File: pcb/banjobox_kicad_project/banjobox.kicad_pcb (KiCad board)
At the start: 2 copper layers, 0 parts

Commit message: added voltage regulator to schematic and finished assigning footprints
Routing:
- removed copper zone on F.Cu, net (none)
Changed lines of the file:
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@@
 		)
 	)
-	(gr_rect
-		(start 131.064 84.328)
-		(end 201.676 121.92)
+	(gr_line
+		(start 51.308 47.244)
+		(end 164.084 33.528)
 		(stroke
-			(width 0.2)
+			(width 0.1)
 			(type default)
 		)
-		(fill no)
-		(layer "F.Cu")
+		(layer "User.1")
 	)
-	(zone
-		(layer "F.Cu")
-		(hatch edge 0.5)
-		(connect_pads
-			(clearance 0.5)
+	(gr_line
+		(start 164.084 33.528)
+		(end 164.084 160.02)
+		(stroke
+			(width 0.1)
+			(type default)
 		)
-		(min_thickness 0.25)
-		(fill
-			(thermal_gap 0.5)
-			(thermal_bridge_width 0.5)
-			(island_removal_mode 1)
+		(layer "User.1")
+	)
+	(gr_line
+		(start 164.084 160.02)
+		(end 51.308 47.244)
+		(stroke
+			(width 0.1)
+			(type default)
 		)
-		(polygon
-			(pts
-				(xy 201.676 84.328) (xy 131.064 84.328) (xy 131.064 121.92) (xy 201.676 121.92)
+		(layer "User.1")
+	)
+	(dimension
+		(type orthogonal)
+		(layer "Edge.Cuts")
+		(pts
+			(xy 164.084 33.528) (xy 164.084 160.02)
+		)
+		(height 11.684)
+		(orientation 1)
+		(format
+			(prefix "")
+			(suffix "")
+			(units 3)
+			(units_format 0)
+			(precision 4)
+			(suppress_zeroes yes)
+		)
+		(style
+			(thickness 0.05)
+			(arrow_length 1.27)
+			(text_position_mode 0)
+			(arrow_direction outward)
+			(extension_height 0.58642)
+			(extension_offset 0.5)
+			(keep_text_aligned yes)
+		)
+		(gr_text "126.492"
+			(at 174.618 96.774 90)
+			(layer "Edge.Cuts")
+			(effects
+				(font
+					(size 1 1)
+					(thickness 0.15)
+				)
 			)
 		)
+	)
+	(dimension
+		(type orthogonal)
+		(layer "User.1")
+		(pts
+			(xy 164.084 160.02) (xy 51.308 47.244)
+		)
+		(height 6.096)
+		(orientation 0)
+		(format
+			(prefix "")
+			(suffix "")
+			(units 3)
+			(units_format 0)
+			(precision 4)
+			(suppress_zeroes yes)
+		)
+		(style
+			(thickness 0.1)
+			(arrow_length 1.27)
+			(text_position_mode 0)
+			(arrow_direction outward)
+			(extension_height 0.58642)
+			(extension_offset 0.5)
+			(keep_text_aligned yes)
+		)
+		(gr_text "112.776"
+			(at 107.696 164.966 0)
+			(layer "User.1")
+			(effects
+				(font
+					(size 1 1)
+					(thickness 0.15)
+				)
+			)
+		)

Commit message: removed R pin from SHT31 to better suit breakout board
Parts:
- added C1: 1uF, Capacitor_THT:CP_Radial_D6.3mm_P2.50mm, F.Cu at (158.8, 117.1)
- added C2: 10uF, Capacitor_THT:CP_Radial_D6.3mm_P2.50mm, F.Cu at (138.5, 130.8)
- added C3: 100nF, Capacitor_THT:C_Disc_D3.4mm_W2.1mm_P2.50mm, F.Cu at (146.8, 136.4)
- added C4: 100nF, Capacitor_THT:C_Disc_D3.4mm_W2.1mm_P2.50mm, F.Cu at (93.5, 83.3)
- added C5: 100nF, Capacitor_THT:C_Disc_D3.4mm_W2.1mm_P2.50mm, F.Cu at (80.3, 59.1)
- added C6: 10uF, Capacitor_THT:CP_Radial_D6.3mm_P2.50mm, F.Cu at (144.8, 72.9)
- added C7: 100uF, Capacitor_THT:CP_Radial_D6.3mm_P2.50mm, F.Cu at (152.9, 73.2)
- added C8: 10uF, Capacitor_THT:CP_Radial_D6.3mm_P2.50mm, F.Cu at (123.5, 91.7)
- added C9: 10uF, Capacitor_THT:CP_Radial_D6.3mm_P2.50mm, F.Cu at (114.8, 95.0)
- added R1: 4.7k, Resistor_THT:R_Axial_DIN0207_L6.3mm_D2.5mm_P7.62mm_Horizontal, F.Cu at (102.9, 71.1)
- added R2: 4.7k, Resistor_THT:R_Axial_DIN0207_L6.3mm_D2.5mm_P7.62mm_Horizontal, F.Cu at (119.4, 71.4)
- added R3: 100k, Resistor_THT:R_Axial_DIN0207_L6.3mm_D2.5mm_P7.62mm_Horizontal, F.Cu at (138.2, 120.1)
- added REF**: TestPoint_THTPad_D3.0mm_Drill1.5mm, TestPoint:TestPoint_THTPad_D3.0mm_Drill1.5mm, F.Cu at (105.2, 94.7)
- added REF**: TestPoint_THTPad_D3.0mm_Drill1.5mm, TestPoint:TestPoint_THTPad_D3.0mm_Drill1.5mm, F.Cu at (101.1, 90.7)
- added RV1: 10K, Potentiometer_THT:Potentiometer_Runtron_RM-065_Vertical, F.Cu at (154.5, 140.5)
- added SW1: RotaryEncoder_Switch, Rotary_Encoder:RotaryEncoder_Alps_EC11E-Switch_Vertical_H20mm, F.Cu at (131.9, 53.1)
- added U2: MOUDLE-SEEEDUINO-XIAO, footprints:XIAO-Generic-Hybrid-14P-2.54-21X17.8MM, B.Cu at (149.9, 90.9)
- added U3: ER_OLEDM0.91_1x-I2C, Display:ER_OLEDM0.91_1x-I2C, F.Cu at (89.4, 59.2)
- added U5: LM1117T-3.3, Package_TO_SOT_THT:TO-220-3_Vertical, F.Cu at (112.5, 83.3)
- added U6: PAM8302AAD, Package_SO:SOIC-8_3.9x4.9mm_P1.27mm, F.Cu at (152.3, 127.9)
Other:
- board text added: "0V"
- board text added: "4.5V"

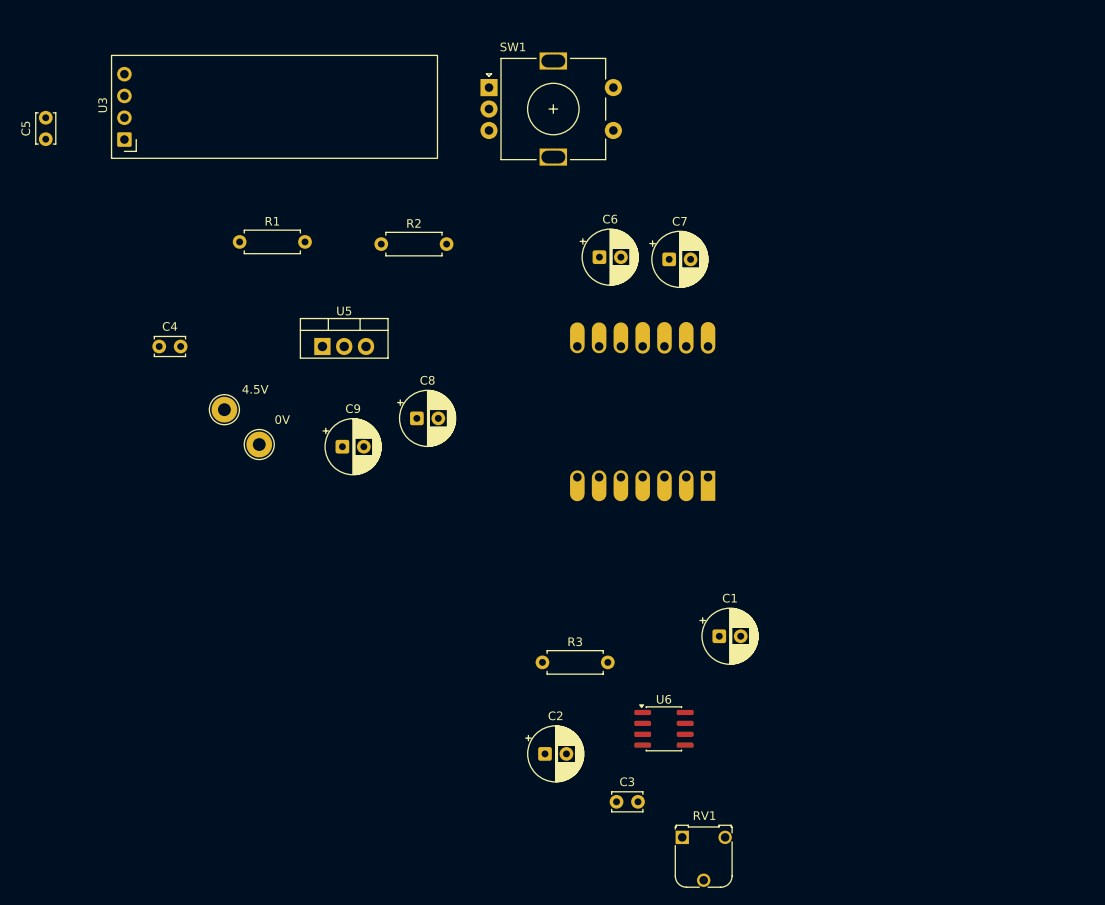
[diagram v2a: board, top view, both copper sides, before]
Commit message: assigned new footprints (pinheader) and more progress on pcb
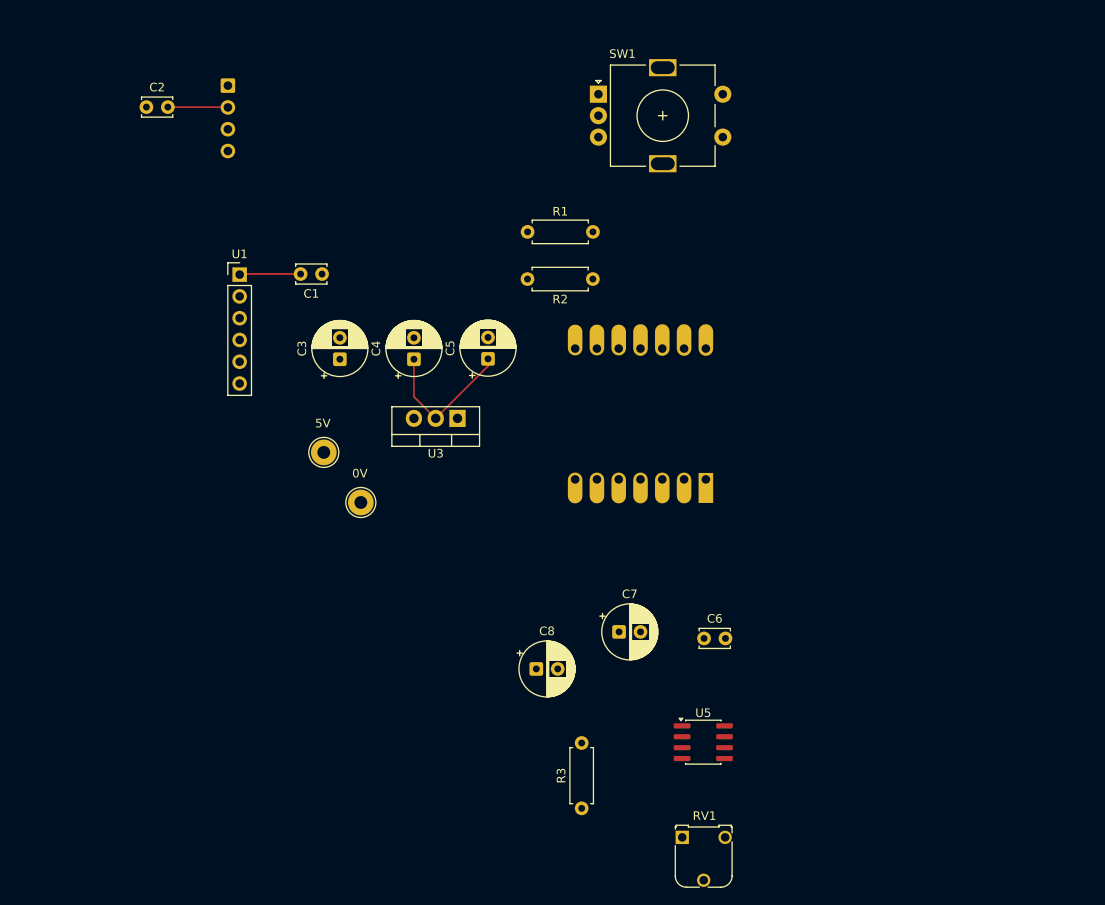
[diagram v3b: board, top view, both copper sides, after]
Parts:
- removed C9: 10uF, Capacitor_THT:CP_Radial_D6.3mm_P2.50mm
- removed U6: PAM8302AAD, Package_SO:SOIC-8_3.9x4.9mm_P1.27mm
- added U1: SHT31-DIS, Connector_PinHeader_2.54mm:PinHeader_1x06_P2.54mm_Vertical, F.Cu at (102.9, 74.9)
- added U4: MOUDLE-SEEEDUINO-XIAO, footprints:XIAO-Generic-Hybrid-14P-2.54-21X17.8MM, B.Cu at (149.6, 91.2)
- C1: value 1uF -> 100nF; footprint Capacitor_THT:CP_Radial_D6.3mm_P2.50mm -> Capacitor_THT:C_Disc_D3.4mm_W2.1mm_P2.50mm
- C2, C6: value 10uF -> 100nF; footprint Capacitor_THT:CP_Radial_D6.3mm_P2.50mm -> Capacitor_THT:C_Disc_D3.4mm_W2.1mm_P2.50mm
- C3, C4: value 100nF -> 10uF; footprint Capacitor_THT:C_Disc_D3.4mm_W2.1mm_P2.50mm -> Capacitor_THT:CP_Radial_D6.3mm_P2.50mm
- C5: value 100nF -> 100uF; footprint Capacitor_THT:C_Disc_D3.4mm_W2.1mm_P2.50mm -> Capacitor_THT:CP_Radial_D6.3mm_P2.50mm
- C7: value 100uF -> 1uF
- U2: value MOUDLE-SEEEDUINO-XIAO -> ER_OLEDM0.91_1x-I2C; footprint footprints:XIAO-Generic-Hybrid-14P-2.54-21X17.8MM -> Display:ER_OLEDM0.91_1x-I2C
- U3: value ER_OLEDM0.91_1x-I2C -> LM1117T-3.3; footprint Display:ER_OLEDM0.91_1x-I2C -> Package_TO_SOT_THT:TO-220-3_Vertical
- U5: value LM1117T-3.3 -> PAM8302AAD; footprint Package_TO_SOT_THT:TO-220-3_Vertical -> Package_SO:SOIC-8_3.9x4.9mm_P1.27mm
- moved C2 88.6 mm to (92.0, 55.4)
- moved U5 64.0 mm to (156.9, 129.4)
- moved C1 62.7 mm to (112.5, 74.9), turned to 180 degrees
- moved U2 61.5 mm to (101.5, 52.9), turned to -90 degrees
- moved C3 60.9 mm to (114.6, 84.8), turned to 90 degrees
- moved C5 57.6 mm to (131.8, 84.8)
- moved U3 50.6 mm to (128.3, 91.7), turned to 180 degrees
- moved C6 46.1 mm to (157.0, 117.3)
- moved C7 43.8 mm to (147.1, 116.6)
- moved R1 33.6 mm to (136.4, 70.0)
- moved C8 32.4 mm to (137.5, 120.9)
- moved C4 29.7 mm to (123.2, 84.8), turned to 90 degrees
- moved R2 25.0 mm to (144.1, 75.5), turned to 180 degrees
- moved R3 17.6 mm to (142.7, 137.2), turned to 90 degrees
- moved REF** 13.6 mm to (117.0, 101.5)
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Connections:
- C1 pad 1: VCC -> GND
- C1 pad 2: GND -> VCC
- C2 pad 1: VCC -> GND
- C2 pad 2: GND -> VCC
- C3 pad 1: PWM -> +5V
- C3 pad 2: Net-(C3-Pad2) -> GND
- C4 pad 1: GND -> VCC
- C4 pad 2: VCC -> GND
- C5 pad 1: GND -> VCC
- C5 pad 2: VCC -> GND
- C6 pad 1: VCC -> PWM
- C6 pad 2: GND -> Net-(C6-Pad2)
- C8 pad 1: +5V -> VCC
- RV1 pad 1: Net-(C3-Pad2) -> Net-(C6-Pad2)
- RV1 pad 2: Net-(U6-IN+) -> Net-(U5-IN+)
- U2 pad 1: EC11A -> GND
- U2 pad 2: EC11B -> VCC
- U2 pad 3: EC11SW1 -> SCL
- U2 pad 4: PWM -> SDA
- U3 pad 3: SCL -> +5V
- U5 pad 1: GND -> unconnected-(U5-~{SD}-Pad1)
- U5 pad 2: VCC -> unconnected-(U5-NC-Pad2)
- U5 pad 3: +5V -> Net-(U5-IN+)
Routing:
- net VCC: track 0.00 -> 31.6 mm
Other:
- board text added: "5V"
- board text removed: "4.5V"

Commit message: forgot to save after last commit, routed pcb
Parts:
- removed the REF** at (117.0, 101.5)
- removed the REF** at (112.7, 95.7)
- added REF**: MountingHole_3.2mm_M3, MountingHole:MountingHole_3.2mm_M3, F.Cu at (91.4, 64.0)
- added REF**: MountingHole_3.2mm_M3, MountingHole:MountingHole_3.2mm_M3, F.Cu at (157.0, 130.6)
- added REF**: MountingHole_3.2mm_M3, MountingHole:MountingHole_3.2mm_M3, F.Cu at (145.8, 67.6)
- added TP1: TestPoint, TestPoint:TestPoint_THTPad_D3.0mm_Drill1.5mm, F.Cu at (109.5, 93.5)
- added TP2: TestPoint, TestPoint:TestPoint_THTPad_D3.0mm_Drill1.5mm, F.Cu at (114.6, 97.3)
- added TP3: TestPoint, TestPoint:TestPoint_THTPad_D3.0mm_Drill1.5mm, F.Cu at (145.0, 126.5)
- added TP4: TestPoint, TestPoint:TestPoint_THTPad_D3.0mm_Drill1.5mm, F.Cu at (152.7, 126.5)
- U2, U4: moved to F.Cu
- moved RV1 36.5 mm to (151.2, 104.2)
- moved R3 23.0 mm to (144.8, 114.3), turned to 0 degrees
- moved U5 19.6 mm to (140.6, 118.6), turned to -90 degrees
- moved C8 16.9 mm to (127.3, 107.4)
- moved C6 16.3 mm to (143.6, 108.1)
- moved C7 14.2 mm to (136.2, 107.4)
- moved U2 6.36 mm to (98.8, 58.7), turned to 90 degrees
- moved U1 5.90 mm to (100.8, 69.4)
- moved C1 5.90 mm to (110.4, 69.3)
- moved R1 3.98 mm to (132.9, 68.2)
- moved R2 3.98 mm to (140.5, 73.7)
- moved U3 3.98 mm to (124.7, 89.9)
- moved C3 3.98 mm to (111.0, 83.0)
- moved C4 3.98 mm to (119.6, 83.0)
- moved C5 3.98 mm to (128.3, 83.0)
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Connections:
- net +5V renamed +BATT
- net GND renamed -BATT
- U4 pad 10: unconnected-(U4-PA5_A9_D9_MISO-Pad10) -> PWM
- U4 pad 4: PWM -> unconnected-(U4-PA11_A3_D3-Pad4)
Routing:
- net VCC: track 31.6 -> 209.8 mm
- net SDA: track 0.00 -> 100.8 mm
- net SCL: track 0.00 -> 84.3 mm
- net EC11A: track 0.00 -> 34.8 mm
- net EC11SW1: track 0.00 -> 32.8 mm
- net EC11B: track 0.00 -> 28.8 mm
- net +BATT: track 0.00 -> 22.8 mm
- net Net-(U5-IN+): track 0.00 -> 18.2 mm
- net PWM: track 0.00 -> 17.8 mm
- net -BATT: track 0.00 -> 15.1 mm, vias 0 -> 4
- net Net-(U5-OUT-): track 0.00 -> 12.4 mm
- net Net-(U5-OUT+): track 0.00 -> 9.15 mm
- net Net-(C6-Pad2): track 0.00 -> 6.70 mm
- added copper zone on B.Cu, net -BATT
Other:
- board outline added: 74.7 x 89.9 mm

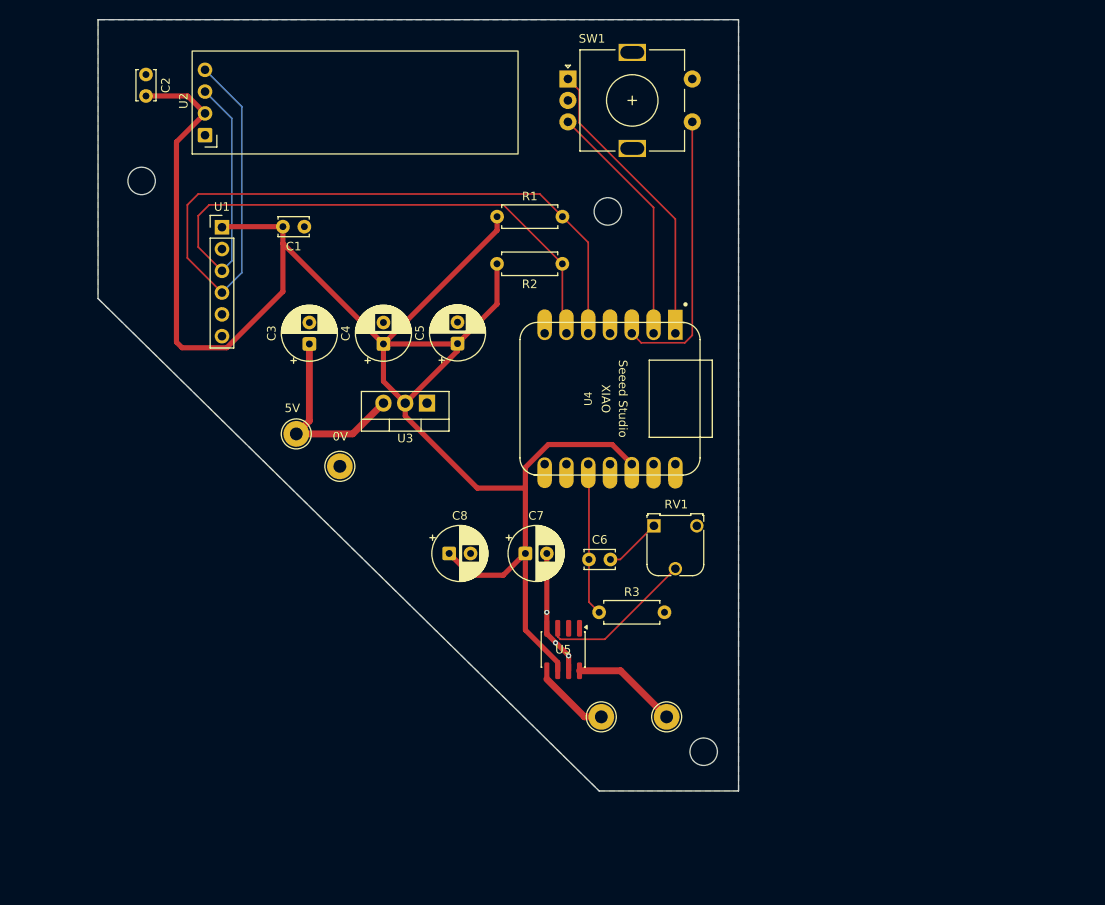
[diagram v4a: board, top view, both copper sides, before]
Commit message: added bird graphic to pcb and added some silkscreen labels
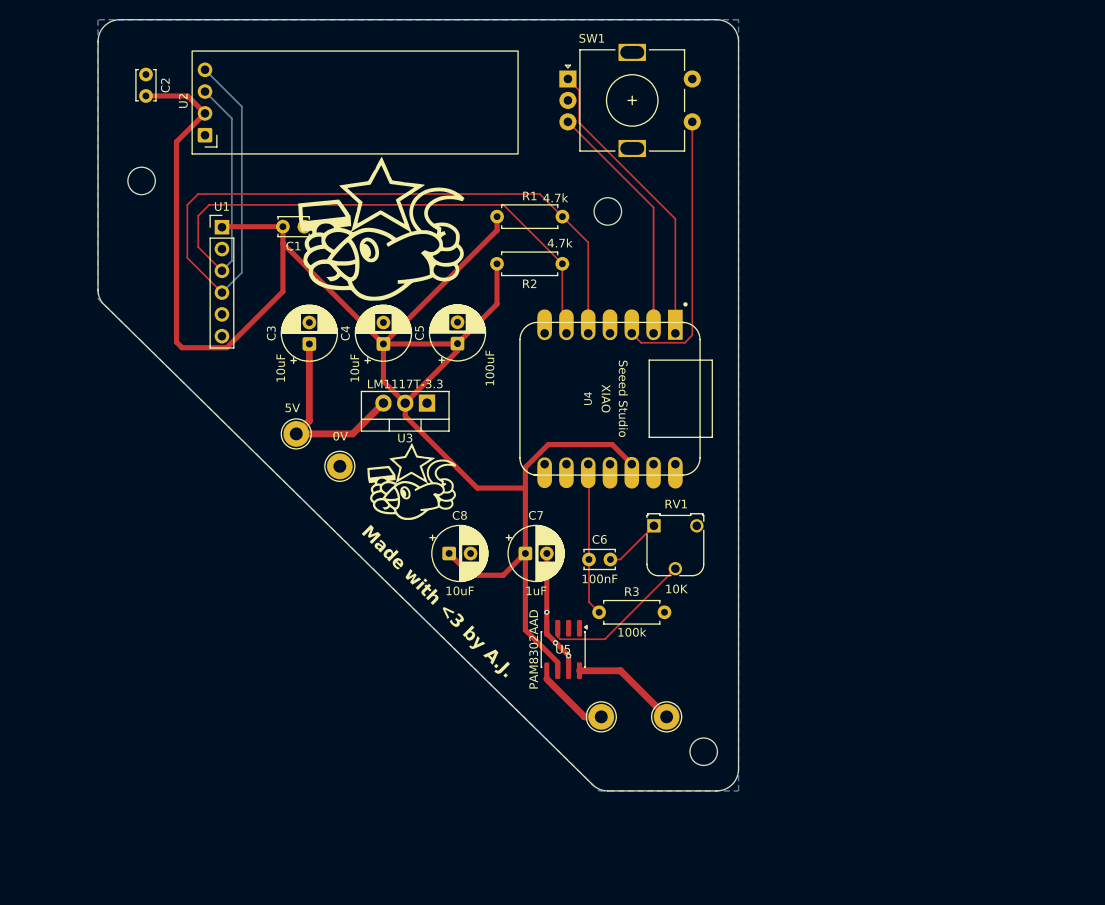
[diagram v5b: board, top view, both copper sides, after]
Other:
- outline, holes or cut-outs redrawn
- board text added: "Banjobox"
- board text added: "Made with <3 by A.J."

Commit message: pcb added all silkscreen text
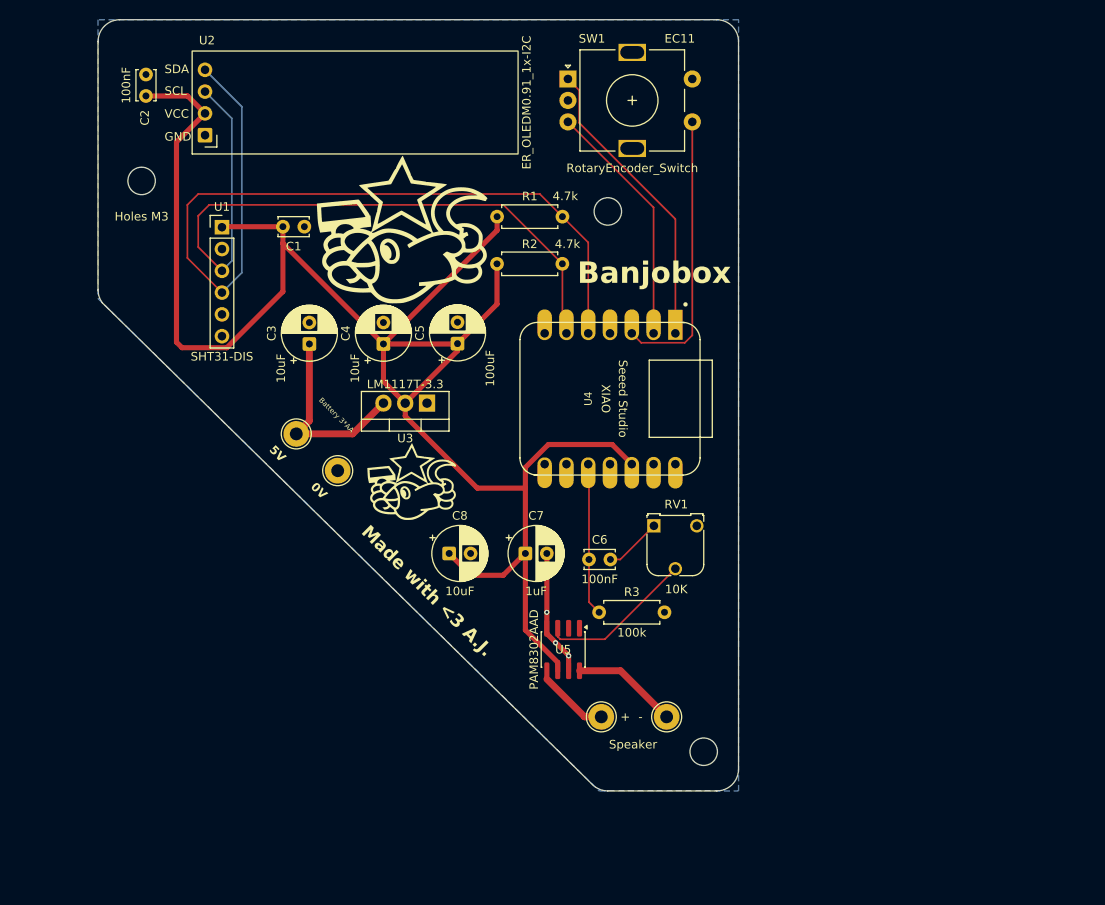
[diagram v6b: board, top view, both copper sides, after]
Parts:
- REF**: value MountingHole_3.2mm_M3 -> Holes M3
- moved TP2 0.57 mm to (114.3, 97.8)
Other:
- board text added: "Battery 3*AA"
- board text added: "EC11"
- board text added: "GND"
- board text added: "Made with <3 A.J."
- board text added: "SCL"
- board text added: "SDA"
- board text added: "Speaker"
- board text added: "VCC"
- board text removed: "Made with <3 by A.J."
